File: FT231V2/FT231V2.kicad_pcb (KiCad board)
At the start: 2 copper layers, 15.2 x 20.3 mm, 24 parts, among them J1 Conn_01x06, P1 USB_C_Plug_USB2.0

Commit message: Soldermask width adjusted
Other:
- rule solder_mask_min_width: 0.1 -> 0.05
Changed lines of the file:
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@@
     (pad_drill 1)
     (pad_to_mask_clearance 0)
-    (solder_mask_min_width 0.1)
+    (solder_mask_min_width 0.05)
     (aux_axis_origin 0 0)
     (visible_elements 7FFFFFFF)

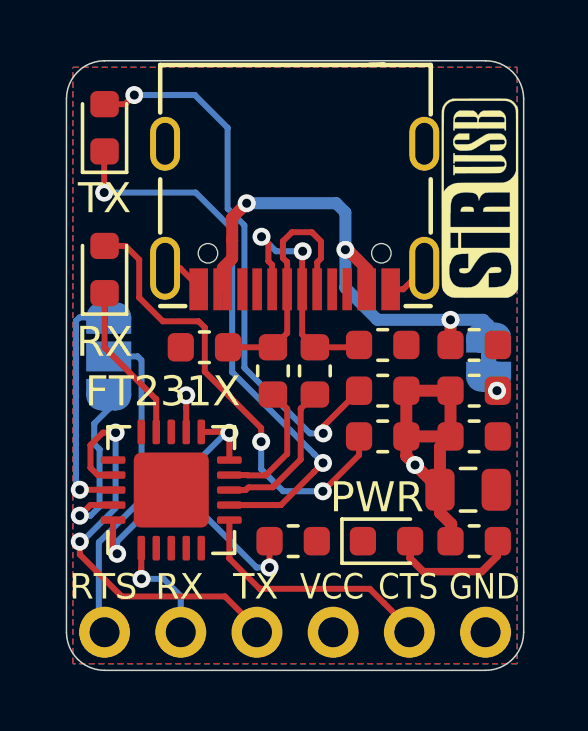
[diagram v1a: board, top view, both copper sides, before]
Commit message: SirUSB Updates
3D Renders changed to white solder mask. CH330N TX and RX references moved
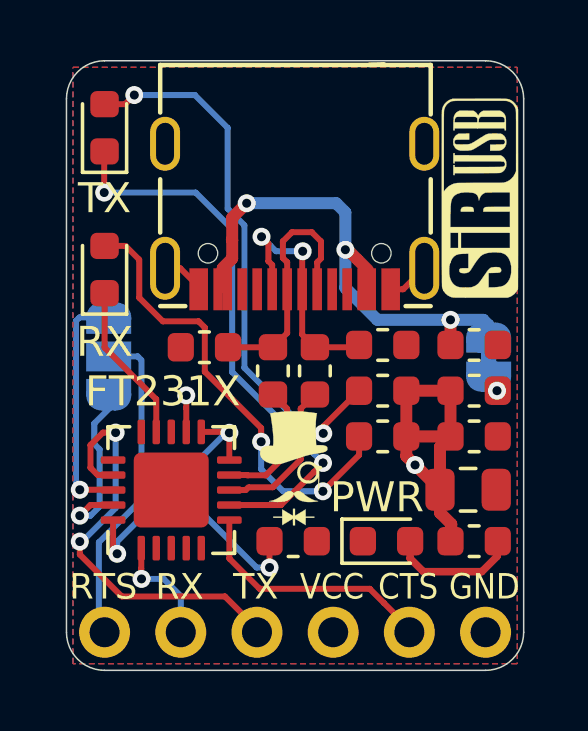
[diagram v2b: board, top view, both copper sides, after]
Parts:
- added G***: LOGO, logo:logo38x53, F.Cu at (64.5, 42.6)

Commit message: SiRUSB Updates
USB-C 3D Renders Added and Pictures Updated
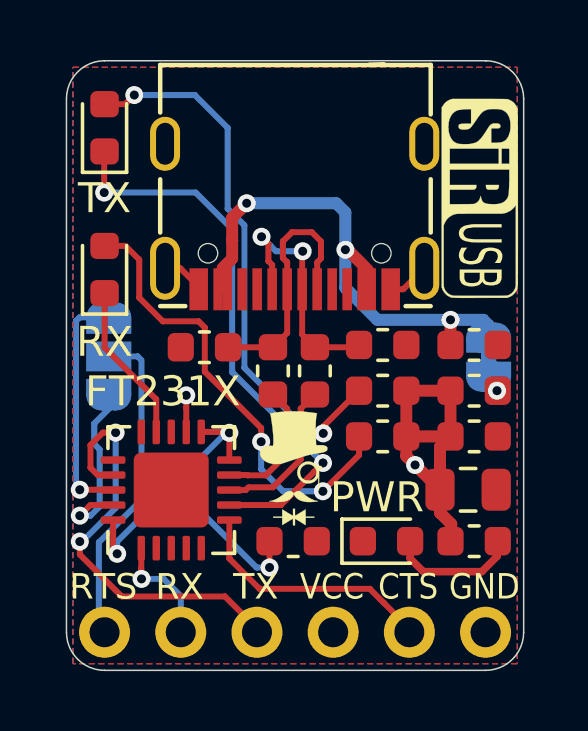
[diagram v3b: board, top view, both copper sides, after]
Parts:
- G***: footprint logo:SirUSB66x25 -> logo:Sir___66x25
- J1: footprint Connector_PinHeader_2.54mm:PinHeader_1x06_P2.54mm_Vertical -> Connector_PinHeader_2.54mm:PinHeader_1x06_P2.54mm_Horizontal
- moved J1 12.7 mm to (70.9, 48.1), turned to 270 degrees
- turned G*** to 270 degrees
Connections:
- J1 pad 1: DTR_RTS -> GND
- J1 pad 2: RX -> CTS
- J1 pad 3: TX -> VCC
- J1 pad 4: VCC -> TX
- J1 pad 5: CTS -> RX
- J1 pad 6: GND -> DTR_RTS
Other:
- board text added: "USB"

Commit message: SirUSB Board Revisions
Removed MicroUSB Versions of FT230 and FT231, SolderPaste Layer Adjusted to -0.05mm, Silkscreens optimised, OSHW logo added.
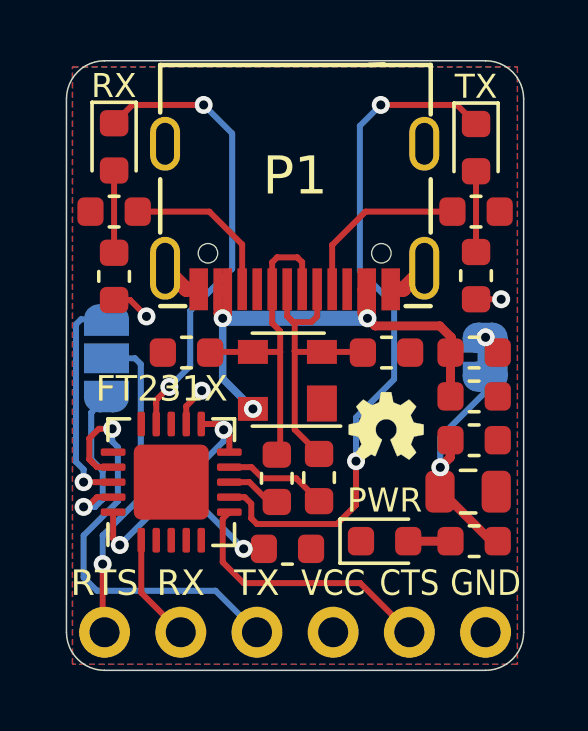
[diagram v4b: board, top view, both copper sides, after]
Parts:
- removed FT231X: FT231XQ, Package_DFN_QFN:QFN-20-1EP_4x4mm_P0.5mm_EP2.5x2.5mm
- removed the G*** at (70.7, 33.6)
- removed the G*** at (64.5, 42.6)
- removed JP2: SolderJumper_3_Open, Jumper:SolderJumper-3_P1.3mm_Open_RoundedPad1.0x1.5mm
- added D1: PRTR5V0U2X, SirBoardLibrary:SOT-143, F.Cu at (64.3, 39.6)
- added G***: LOGO, logo:OSHW36x26, F.Cu at (67.6, 41.2)
- added P6: SolderJumper_3_Open, Jumper:SolderJumper-3_P1.3mm_Open_RoundedPad1.0x1.5mm, B.Cu at (58.3, 38.9)
- added R6: 5k1, Resistor_SMD:R_0603_1608Metric, F.Cu at (58.5, 34.0)
- added R7: 5k1, Resistor_SMD:R_0603_1608Metric, F.Cu at (70.6, 34.0)
- added U1: FT231XQ, Package_DFN_QFN:QFN-20-1EP_4x4mm_P0.5mm_EP2.5x2.5mm, F.Cu at (60.5, 43.1)
- R3, R4, R5: value 680E -> 1k
- moved TX 12.4 mm to (70.6, 31.9), turned to 270 degrees
- moved R5 10.4 mm to (58.5, 36.2), turned to 90 degrees
- moved C2 6.55 mm to (61.0, 38.7), turned to 180 degrees
- moved C3 6.07 mm to (67.6, 38.7), turned to 0 degrees
- moved R3 4.94 mm to (70.6, 36.2), turned to 90 degrees
- moved RX 4.10 mm to (58.5, 31.9), turned to 270 degrees
- moved R1 3.87 mm to (65.4, 42.9)
- moved R2 3.80 mm to (64.0, 42.9)
- moved C1 1.71 mm to (70.5, 40.2)
- moved FB1 1.27 mm to (70.5, 38.7), turned to 180 degrees
- moved REF** 0.44 mm to (64.6, 43.1)
- moved C6 0.32 mm to (64.3, 45.3)
- moved G*** 0.25 mm to (64.6, 38.6)
- moved G*** 0.13 mm to (64.6, 33.7)
- moved C4 0.13 mm to (70.5, 41.7)
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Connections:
- net /D+ renamed D+
- net /D- renamed D-
- C1 pad 1: /VUSB -> VUSB
- FB1 pad 1: VCC -> Net-(FB1-Pad1)
- FB1 pad 2: Net-(FB1-Pad2) -> VUSB
- J1 pad 6: DTR_RTS -> P6
- JP1 pad 1: /VUSB -> Net-(FB1-Pad1)
- JP1 pad 2: Net-(FB1-Pad2) -> VCC
- P1 pad A4: /VUSB -> VUSB
- P1 pad A9: /VUSB -> VUSB
- P1 pad B4: /VUSB -> VUSB
- P1 pad B9: /VUSB -> VUSB
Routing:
- net VUSB: track 0.00 -> 18.0 mm, vias 0 -> 3
- net /VUSB: track 17.4 -> 0.00 mm, vias 3 -> 0
- net Net-(R3-Pad2): track 18.4 -> 2.69 mm, vias 2 -> 0
- net Net-(R5-Pad2): track 15.4 -> 2.74 mm, vias 2 -> 0
- net DTR_RTS: track 10.9 -> 0.00 mm
- net P6: track 0.00 -> 10.7 mm, vias 0 -> 1
- net CBUS1: track 5.34 -> 15.3 mm, vias 0 -> 2
- net Net-(P1-PadA5): track 0.00 -> 5.94 mm
- net Net-(P1-PadB5): track 0.00 -> 5.43 mm
- net CBUS2: track 18.9 -> 23.2 mm
- net Net-(PWR1-Pad2): track 4.38 -> 1.41 mm
- net uD+: track 5.11 -> 2.17 mm
- net D+: track 8.26 -> 11.0 mm, vias 2 -> 0
- net Net-(C6-Pad1): track 13.9 -> 11.8 mm
- net D-: track 8.46 -> 10.3 mm
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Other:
- board text added: "FT231X"
- board text added: "www.SirBoard.com"
- board text removed: "USB"
